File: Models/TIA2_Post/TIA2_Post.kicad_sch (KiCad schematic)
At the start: 0 parts

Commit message: Save progress
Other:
- note added: "Input: 15V power Input: -15V power Input: AD8615 output Output: post voltage Input to board: pre voltage Ground connection(s) not yet elaborated"
- note removed: "Input: 15V power Input: -15V power Input: AD8615 output Output: post voltage"
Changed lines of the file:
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@@
 	(generator_version "9.0")
 	(paper "A4")
-	(text "Input: 15V power\nInput: -15V power\nInput: AD8615 output\nOutput: post voltage"
+	(text "Input: 15V power\nInput: -15V power\nInput: AD8615 output\nOutput: post voltage\n\nInput to board: pre voltage\n\nGround connection(s) not yet elaborated"
 		(exclude_from_sim no)
-		(at 172.212 103.124 0)
+		(at 158.242 76.962 0)
 		(effects
 			(font
@@
 	)
 	(sheet
-		(at 127 101.6)
-		(size 40.64 30.48)
+		(at 101.6 76.2)
+		(size 50.8 50.8)
 		(exclude_from_sim no)
 		(in_bom yes)
@@
 		)
 		(property "Sheetname" "Amplifier"
-			(at 127 100.8884 0)
+			(at 101.6 75.4884 0)
 			(effects
 				(font
@@
 		)
 		(property "Sheetfile" "Amplifier.kicad_sch"
-			(at 127 132.6646 0)
+			(at 101.6 127.5846 0)
 			(effects
 				(font
@@
 		)
 		(instances
-			(project "PowerBoard"
-				(path "/c19e9b7b-7f36-470c-862a-1a648d3f14f6/3c1c1dcd-dbca-4c3e-a9c0-5c49f174be9d"
-					(page "7")
+			(project "TIA2_Post"
+				(path "/f19129fc-f916-4692-924c-ee308c6b3e1d"
+					(page "2")
 				)
 			)
 		)
 	)
+	(sheet_instances
+		(path "/"
+			(page "1")
+		)
+	)
+	(embedded_fonts no)
 )

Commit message: Save progress
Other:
- added sheet CompensationNetwork (CompensationNetwork.kicad_sch)
- note added: "Input: 15V power Input: -15V power Input: AD8615 output Output: post voltage"
- note added: "Input: pre voltage Output: post voltage"
- note removed: "Input: 15V power Input: -15V power Input: AD8615 output Output: post voltage Input to board: pre voltage Ground connection(s) not yet elaborated"
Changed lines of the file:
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@@
 	(generator_version "9.0")
 	(paper "A4")
-	(text "Input: 15V power\nInput: -15V power\nInput: AD8615 output\nOutput: post voltage\n\nInput to board: pre voltage\n\nGround connection(s) not yet elaborated"
+	(text "Input: 15V power\nInput: -15V power\nInput: AD8615 output\nOutput: post voltage"
 		(exclude_from_sim no)
-		(at 158.242 76.962 0)
+		(at 158.242 102.362 0)
+		(effects
+			(font
+				(size 1.27 1.27)
+			)
+			(justify left top)
+		)
+	)
+	(text "Input: pre voltage\nOutput: post voltage"
+		(exclude_from_sim no)
+		(at 155.194 51.562 0)
 		(effects
 			(font
@@
 	)
 	(sheet
-		(at 101.6 76.2)
-		(size 50.8 50.8)
+		(at 101.6 101.6)
+		(size 50.8 25.4)
 		(exclude_from_sim no)
 		(in_bom yes)
@@
 		)
 		(property "Sheetname" "Amplifier"
-			(at 101.6 75.4884 0)
+			(at 101.6 100.8884 0)
 			(effects
 				(font
@@
 				)
 			)
+		)
+	)
+	(sheet
+		(at 101.6 50.8)
+		(size 50.8 25.4)
+		(exclude_from_sim no)
+		(in_bom yes)
+		(on_board yes)
+		(dnp no)
+		(fields_autoplaced yes)
+		(stroke
+			(width 0.1524)
+			(type solid)
+		)
+		(fill
+			(color 0 0 0 0.0000)
+		)
+		(property "Sheetname" "CompensationNetwork"
+			(at 101.6 50.0884 0)
+			(effects
+				(font
+					(size 1.27 1.27)
+				)
+				(justify left bottom)
+			)
+		)
+		(property "Sheetfile" "CompensationNetwork.kicad_sch"
+			(at 101.6 76.7846 0)
+			(effects
+				(font
+					(size 1.27 1.27)
+				)
+				(justify left top)
+			)
+		)
+		(instances
+			(project "TIA2_Post"
+				(path "/f19129fc-f916-4692-924c-ee308c6b3e1d"
+					(page "3")
+				)
+			)

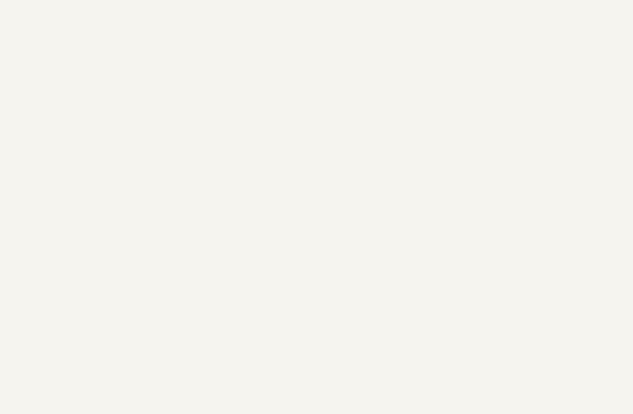
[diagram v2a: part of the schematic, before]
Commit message: Finished with the chips for the transimpedance amplifiers
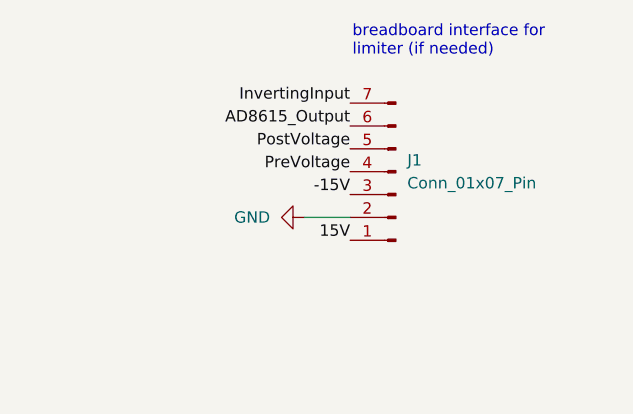
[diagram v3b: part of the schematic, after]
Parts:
- added J1: Conn_01x07_Pin, symbol Connector:Conn_01x07_Pin
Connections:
- new net -15V: J1.3 (Pin_3)
- new net 15V: J1.1 (Pin_1)
- new net AD8615_Output: J1.6 (Pin_6)
- new net GND: J1.2 (Pin_2)
- new net InvertingInput: J1.7 (Pin_7)
- new net PostVoltage: J1.5 (Pin_5)
- new net PreVoltage: J1.4 (Pin_4)
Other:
- note added: "breadboard interface for limiter (if needed)"
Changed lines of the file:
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@@
 	(generator_version "9.0")
 	(paper "A4")
+	(text "breadboard interface for\nlimiter (if needed)"
+		(exclude_from_sim no)
+		(at 254.254 42.164 0)
+		(effects
+			(font
+				(size 1.27 1.27)
+			)
+			(justify left top)
+		)
+	)
 	(text "Input: 15V power\nInput: -15V power\nInput: AD8615 output\nOutput: post voltage"
 		(exclude_from_sim no)
@@
 		)
 	)
+	(wire
+		(pts
+			(xy 248.92 63.5) (xy 254 63.5)
+		)
+		(stroke
+			(width 0)
+			(type default)
+		)
+	)
+	(label "InvertingInput"
+		(at 254 50.8 180)
+		(effects
+			(font
+				(size 1.27 1.27)
+			)
+			(justify right bottom)
+		)
+	)
+	(label "PreVoltage"
+		(at 254 58.42 180)
+		(effects
+			(font
+				(size 1.27 1.27)
+			)
+			(justify right bottom)
+		)
+	)
+	(label "PostVoltage"
+		(at 254 55.88 180)
+		(effects
+			(font
+				(size 1.27 1.27)
+			)
+			(justify right bottom)
+		)
+	)
+	(label "AD8615_Output"
+		(at 254 53.34 180)
+		(effects
+			(font
+				(size 1.27 1.27)
+			)
+			(justify right bottom)
+		)
+	)
+	(label "15V"
+		(at 254 66.04 180)
+		(effects
+			(font
+				(size 1.27 1.27)
+			)
+			(justify right bottom)
+		)
+	)
+	(label "-15V"
+		(at 254 60.96 180)
+		(effects
+			(font
+				(size 1.27 1.27)
+			)
+			(justify right bottom)
+		)
+	)
+	(symbol
+		(lib_id "power:GND")
+		(at 248.92 63.5 270)
+		(unit 1)
+		(exclude_from_sim no)
+		(in_bom yes)
+		(on_board yes)
+		(dnp no)
+		(fields_autoplaced yes)
+		(property "Reference" "#PWR05"
+			(at 242.57 63.5 0)
+			(effects
+				(font
+					(size 1.27 1.27)
+				)
+				(hide yes)
+			)
+		)
+		(property "Value" "GND"
+			(at 245.11 63.4999 90)
+			(effects
+				(font
+					(size 1.27 1.27)
+				)
+				(justify right)
+			)
+		)
+		(property "Footprint" ""
+			(at 248.92 63.5 0)
+			(effects
+				(font
+					(size 1.27 1.27)
+				)
+				(hide yes)
+			)
+		)
+		(property "Datasheet" ""
+			(at 248.92 63.5 0)
+			(effects
+				(font
+					(size 1.27 1.27)
+				)
+				(hide yes)
+			)
+		)
+		(property "Description" "Power symbol creates a global label with name \"GND\" , ground"
+			(at 248.92 63.5 0)
+			(effects
+				(font
+					(size 1.27 1.27)
+				)
+				(hide yes)
+			)
+		)
+		(pin "1"
+		)
+		(instances
+			(project ""
+				(path "/f19129fc-f916-4692-924c-ee308c6b3e1d"
+					(reference "#PWR05")
+					(unit 1)
+				)
+			)
+		)
+	)
+	(symbol
+		(lib_id "Connector:Conn_01x07_Pin")
+		(at 259.08 58.42 180)
+		(unit 1)
+		(exclude_from_sim no)
+		(in_bom yes)
+		(on_board yes)
+		(dnp no)
+		(fields_autoplaced yes)
+		(property "Reference" "J1"
+			(at 260.35 57.1499 0)
+			(effects
+				(font
+					(size 1.27 1.27)
+				)
+				(justify right)
+			)
+		)
+		(property "Value" "Conn_01x07_Pin"
+			(at 260.35 59.6899 0)
+			(effects
+				(font
+					(size 1.27 1.27)
+				)
+				(justify right)
+			)
+		)
+		(property "Footprint" ""
+			(at 259.08 58.42 0)
+			(effects
+				(font
+					(size 1.27 1.27)
+				)
+				(hide yes)
+			)
+		)
+		(property "Datasheet" "~"
+			(at 259.08 58.42 0)
+			(effects
+				(font
+					(size 1.27 1.27)
+				)
+				(hide yes)
+			)
+		)
+		(property "Description" "Generic connector, single row, 01x07, script generated"
+			(at 259.08 58.42 0)
+			(effects
+				(font
+					(size 1.27 1.27)
+				)
+				(hide yes)
+			)
+		)
+		(pin "1"
+		)
+		(pin "2"
+		)
+		(pin "3"
+		)
+		(pin "4"
+		)
+		(pin "5"
+		)
+		(pin "6"
+		)
+		(pin "7"
+		)
+		(instances
+			(project ""
+				(path "/f19129fc-f916-4692-924c-ee308c6b3e1d"
+					(reference "J1")
+					(unit 1)
+				)
+			)
+		)
+	)

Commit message: Save progress
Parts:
- removed J1: Conn_01x07_Pin, symbol Connector:Conn_01x07_Pin
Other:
- added sheet Limiter (Limiter.kicad_sch)
- note removed: "breadboard interface for limiter (if needed)"
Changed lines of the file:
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@@
 	(generator_version "9.0")
 	(paper "A4")
-	(text "breadboard interface for\nlimiter (if needed)"
-		(exclude_from_sim no)
-		(at 254.254 42.164 0)
-		(effects
-			(font
-				(size 1.27 1.27)
-			)
-			(justify left top)
-		)
-	)
 	(text "Input: 15V power\nInput: -15V power\nInput: AD8615 output\nOutput: post voltage"
 		(exclude_from_sim no)
@@
 		)
 	)
-	(wire
-		(pts
-			(xy 248.92 63.5) (xy 254 63.5)
-		)
-		(stroke
-			(width 0)
-			(type default)
-		)
-	)
-	(label "InvertingInput"
-		(at 254 50.8 180)
-		(effects
-			(font
-				(size 1.27 1.27)
-			)
-			(justify right bottom)
-		)
-	)
-	(label "PreVoltage"
-		(at 254 58.42 180)
-		(effects
-			(font
-				(size 1.27 1.27)
-			)
-			(justify right bottom)
-		)
-	)
-	(label "PostVoltage"
-		(at 254 55.88 180)
-		(effects
-			(font
-				(size 1.27 1.27)
-			)
-			(justify right bottom)
-		)
-	)
-	(label "AD8615_Output"
-		(at 254 53.34 180)
-		(effects
-			(font
-				(size 1.27 1.27)
-			)
-			(justify right bottom)
-		)
-	)
-	(label "15V"
-		(at 254 66.04 180)
-		(effects
-			(font
-				(size 1.27 1.27)
-			)
-			(justify right bottom)
-		)
-	)
-	(label "-15V"
-		(at 254 60.96 180)
-		(effects
-			(font
-				(size 1.27 1.27)
-			)
-			(justify right bottom)
-		)
-	)
-	(symbol
-		(lib_id "power:GND")
-		(at 248.92 63.5 270)
-		(unit 1)
+	(sheet
+		(at 203.2 50.8)
+		(size 50.8 25.4)
 		(exclude_from_sim no)
 		(in_bom yes)
@@
 		(dnp no)
 		(fields_autoplaced yes)
-		(property "Reference" "#PWR05"
-			(at 242.57 63.5 0)
+		(stroke
+			(width 0.1524)
+			(type solid)
+		)
+		(fill
+			(color 0 0 0 0.0000)
+		)
+		(property "Sheetname" "Limiter"
+			(at 203.2 50.0884 0)
 			(effects
 				(font
 					(size 1.27 1.27)
 				)
-				(hide yes)
+				(justify left bottom)
 			)
 		)
-		(property "Value" "GND"
-			(at 245.11 63.4999 90)
+		(property "Sheetfile" "Limiter.kicad_sch"
+			(at 203.2 76.7846 0)
 			(effects
 				(font
 					(size 1.27 1.27)
 				)
-				(justify right)
+				(justify left top)
 			)
 		)
-		(property "Footprint" ""
-			(at 248.92 63.5 0)
-			(effects
-				(font
-					(size 1.27 1.27)
-				)
-				(hide yes)
-			)
-		)
-		(property "Datasheet" ""
-			(at 248.92 63.5 0)
-			(effects
-				(font
-					(size 1.27 1.27)
-				)
-				(hide yes)
-			)
-		)
-		(property "Description" "Power symbol creates a global label with name \"GND\" , ground"
-			(at 248.92 63.5 0)
-			(effects
-				(font
-					(size 1.27 1.27)
-				)
-				(hide yes)
-			)
-		)
-		(pin "1"
-		)
 		(instances
-			(project ""
+			(project "TIA2_Post"
 				(path "/f19129fc-f916-4692-924c-ee308c6b3e1d"
-					(reference "#PWR05")
-					(unit 1)
+					(page "4")
 				)
 			)
-		)
-	)
-	(symbol
-		(lib_id "Connector:Conn_01x07_Pin")
-		(at 259.08 58.42 180)
-		(unit 1)
-		(exclude_from_sim no)
-		(in_bom yes)
-		(on_board yes)
-		(dnp no)
-		(fields_autoplaced yes)
-		(property "Reference" "J1"
-			(at 260.35 57.1499 0)
-			(effects
-				(font
-					(size 1.27 1.27)
-				)
-				(justify right)
-			)
-		)
-		(property "Value" "Conn_01x07_Pin"
-			(at 260.35 59.6899 0)
-			(effects
-				(font
-					(size 1.27 1.27)
-				)
-				(justify right)
-			)
-		)
-		(property "Footprint" ""
-			(at 259.08 58.42 0)
-			(effects
-				(font
-					(size 1.27 1.27)
-				)
-				(hide yes)
-			)
-		)
-		(property "Datasheet" "~"
-			(at 259.08 58.42 0)
-			(effects
-				(font
-					(size 1.27 1.27)
-				)
-				(hide yes)
-			)
-		)
-		(property "Description" "Generic connector, single row, 01x07, script generated"
-			(at 259.08 58.42 0)
-			(effects
-				(font
-					(size 1.27 1.27)
-				)
-				(hide yes)
-			)
-		)
-		(pin "1"
-		)
-		(pin "2"
-		)
-		(pin "3"
-		)
-		(pin "4"
-		)
-		(pin "5"
-		)
-		(pin "6"
-		)
-		(pin "7"
-		)
-		(instances
-			(project ""
-				(path "/f19129fc-f916-4692-924c-ee308c6b3e1d"
-					(reference "J1")
-					(unit 1)
-				)
-			)

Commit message: Save progress
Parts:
- added J3: Conn_01x03_Pin, symbol Connector:Conn_01x03_Pin
- added R1: 10, symbol Device:R_US
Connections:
- new net: J3.1 (Pin_1), R1.1
- new net GND: J3.3 (Pin_3), R1.2
- new net ISO_GND: J3.2 (Pin_2)
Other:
- sheet Amplifier ports: added AD8615_Output, InvertingInput, PostVoltage; removed none
- sheet CompensationNetwork ports: added PostVoltage, PreVoltage; removed none
- sheet Limiter ports: added InvertingInput, PostVoltage; removed none
- note removed: "Input: 15V power Input: -15V power Input: AD8615 output Output: post voltage"
- note removed: "Input: pre voltage Output: post voltage"

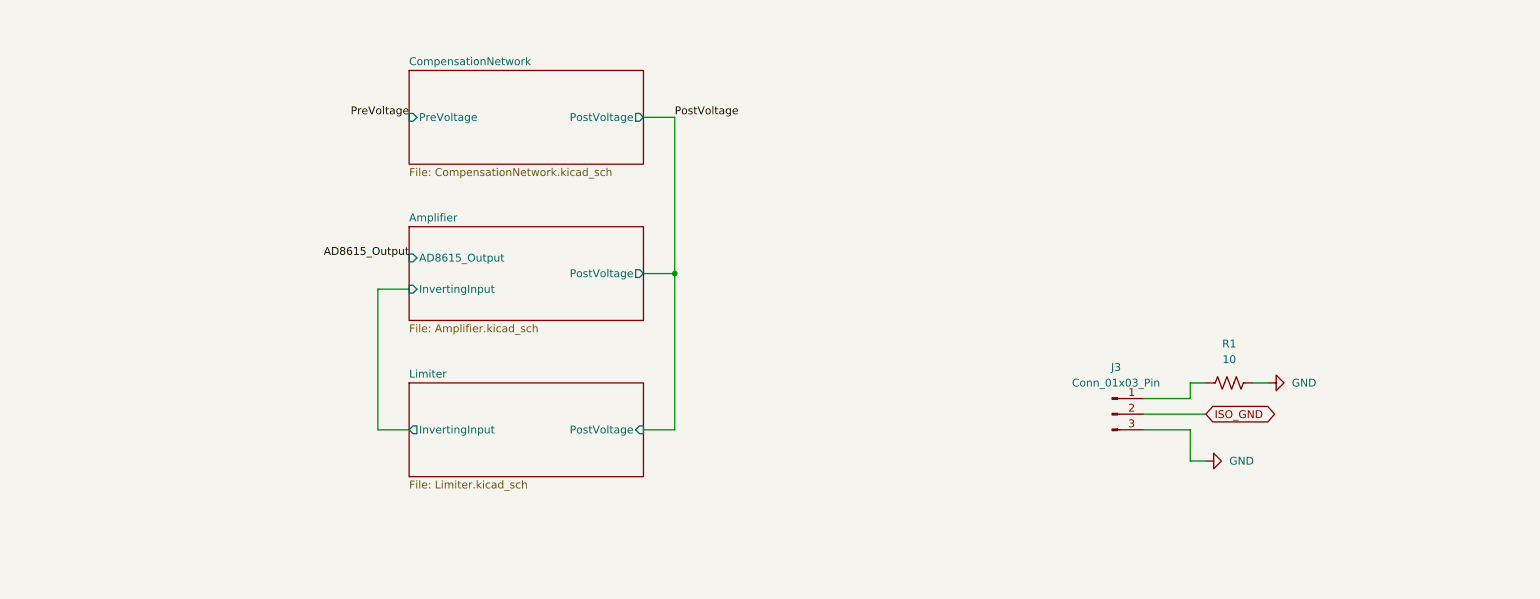
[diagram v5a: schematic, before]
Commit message: ERC passes for the two new boards
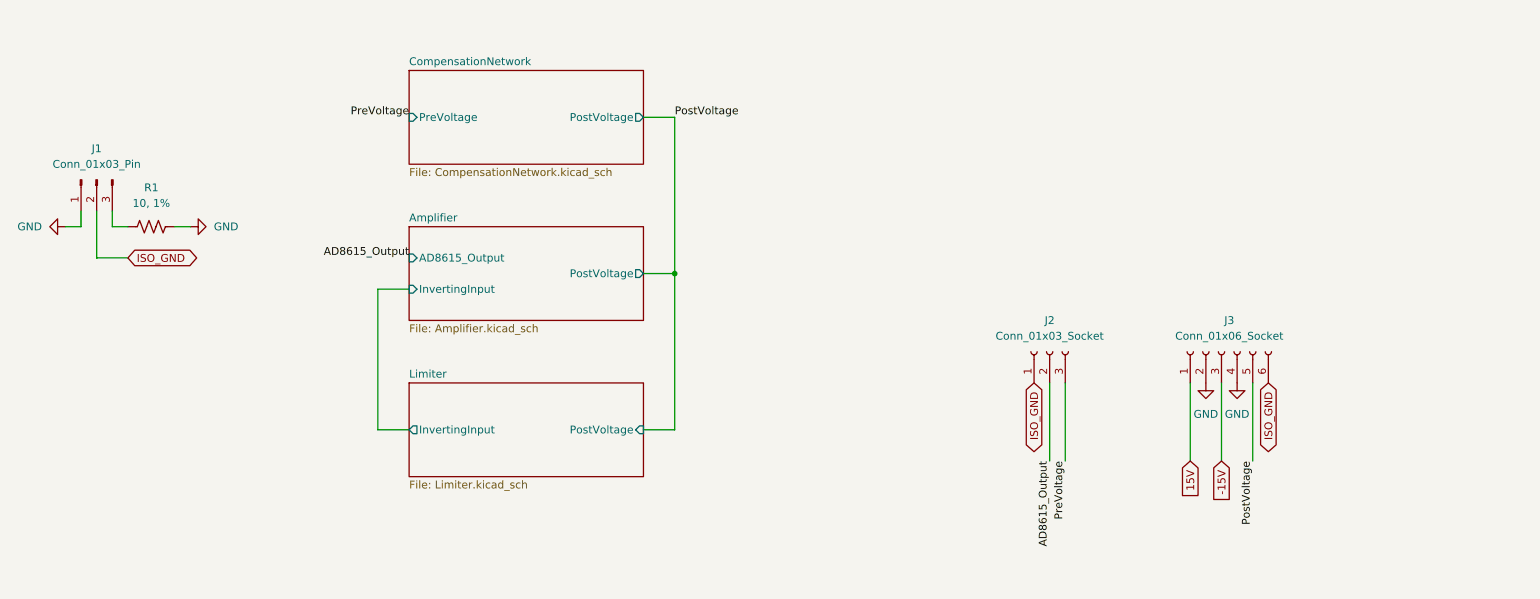
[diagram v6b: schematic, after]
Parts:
- removed J3: Conn_01x03_Pin, symbol Connector:Conn_01x03_Pin
- added J1: Conn_01x03_Pin, Connector_Custom:PinHeader_1x3, symbol Connector:Conn_01x03_Pin
- added J2: Conn_01x03_Socket, Connector_Custom:PinSocket_1x3, symbol Connector:Conn_01x03_Socket
- added J3: Conn_01x06_Socket, Connector_Custom:PinSocket_1x6, symbol Connector:Conn_01x06_Socket
- R1: value 10 -> 10, 1%; footprint (none) -> TwoTerminal:RESC0603; Cost (none) -> $0.030; Purchase Link (none) -> https://www.digikey.com/en/products/detail/vishay-dale/CRCW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
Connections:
- net AD8615_Output: now also J2.2 (Pin_2)
- net GND: now also J1.1 (Pin_1), J3.2 (Pin_2), J3.4 (Pin_4)
- net ISO_GND: now also J1.2 (Pin_2), J2.1 (Pin_1), J3.6 (Pin_6)
- net PostVoltage: now also J3.5 (Pin_5)
- net PreVoltage: now also J2.3 (Pin_3)
- net at R1.1: now also J1.3 (Pin_3)
- new net -15V: J3.3 (Pin_3)
- new net 15V: J3.1 (Pin_1)

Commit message: First time that all PCBs are fully wired
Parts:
- added H1, H2: MountingHole, Connector_Custom:DowelPin_2.5mm, symbol Mechanical:MountingHole
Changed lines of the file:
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@@
+	)
+	(symbol
+		(lib_id "Mechanical:MountingHole")
+		(at 223.52 55.88 0)
+		(unit 1)
+		(exclude_from_sim no)
+		(in_bom no)
+		(on_board yes)
+		(dnp no)
+		(fields_autoplaced yes)
+		(property "Reference" "H2"
+			(at 226.06 54.6099 0)
+			(effects
+				(font
+					(size 1.27 1.27)
+				)
+				(justify left)
+			)
+		)
+		(property "Value" "MountingHole"
+			(at 226.06 57.1499 0)
+			(effects
+				(font
+					(size 1.27 1.27)
+				)
+				(justify left)
+			)
+		)
+		(property "Footprint" "Connector_Custom:DowelPin_2.5mm"
+			(at 223.52 55.88 0)
+			(effects
+				(font
+					(size 1.27 1.27)
+				)
+				(hide yes)
+			)
+		)
+		(property "Datasheet" "~"
+			(at 223.52 55.88 0)
+			(effects
+				(font
+					(size 1.27 1.27)
+				)
+				(hide yes)
+			)
+		)
+		(property "Description" "Mounting Hole without connection"
+			(at 223.52 55.88 0)
+			(effects
+				(font
+					(size 1.27 1.27)
+				)
+				(hide yes)
+			)
+		)
+		(instances
+			(project "TIA2_Post"
+				(path "/f19129fc-f916-4692-924c-ee308c6b3e1d"
+					(reference "H2")
+					(unit 1)
+				)
+			)
+		)
 	)
 	(symbol
@@
 					(unit 1)
 				)
+			)
+		)
+	)
+	(symbol
+		(lib_id "Mechanical:MountingHole")
+		(at 203.2 55.88 0)
+		(unit 1)
+		(exclude_from_sim no)
+		(in_bom no)
+		(on_board yes)
+		(dnp no)
+		(fields_autoplaced yes)
+		(property "Reference" "H1"
+			(at 205.74 54.6099 0)
+			(effects
+				(font
+					(size 1.27 1.27)
+				)
+				(justify left)
+			)
+		)
+		(property "Value" "MountingHole"
+			(at 205.74 57.1499 0)
+			(effects
+				(font
+					(size 1.27 1.27)
+				)
+				(justify left)
+			)
+		)
+		(property "Footprint" "Connector_Custom:DowelPin_2.5mm"
+			(at 203.2 55.88 0)
+			(effects
+				(font
+					(size 1.27 1.27)
+				)
+				(hide yes)
+			)
+		)
+		(property "Datasheet" "~"
+			(at 203.2 55.88 0)
+			(effects
+				(font
+					(size 1.27 1.27)
+				)
+				(hide yes)
+			)
+		)
+		(property "Description" "Mounting Hole without connection"
+			(at 203.2 55.88 0)
+			(effects
+				(font
+					(size 1.27 1.27)
+				)
+				(hide yes)
+			)
+		)
+		(property "Purchase Link" ""
+			(at 203.2 55.88 0)
+			(effects
+				(font
+					(size 1.27 1.27)
+				)
+				(hide yes)
+			)
+		)
+		(instances
+			(project ""
+				(path "/f19129fc-f916-4692-924c-ee308c6b3e1d"
+					(reference "H1")
+					(unit 1)
+				)

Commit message: Save progress
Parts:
- J1, R1: now left out of the parts list
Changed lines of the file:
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@@
 		(unit 1)
 		(exclude_from_sim no)
-		(in_bom yes)
+		(in_bom no)
 		(on_board yes)
 		(dnp no)
@@
 		(unit 1)
 		(exclude_from_sim no)
-		(in_bom yes)
-		(on_board yes)
-		(dnp no)
+		(in_bom no)
+		(on_board yes)
+		(dnp no)
